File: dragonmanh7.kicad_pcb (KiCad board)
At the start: 4 copper layers, 135.6 x 54.6 mm, 110 parts, among them J1 USB_B, J10 Conn_02x12_Odd_Even, J11 Conn_02x03_Odd_Even, J12 VBAT+, J13 Conn_02x05_Odd_Even, J14 VBATG, J15 Conn_02x02_Odd_Even, J18 Conn_02x05_Odd_Even, J2 73725-0110BLF, J3 RJ45_Amphenol_RJMG1BD3B8K1ANR, J4 Micro_SD_Card, J5 Screw_Terminal_01x06, J6 Conn_02x12_Odd_Even, J7 USB_B, J8 Screw_Terminal_01x02, J9 Conn_02x12_Odd_Even, SW1 RESET, SW2 PC13, U1 STM32H743VITx, U10 USBLC6-2SC6, U12 TCAN332, U13 ISL83483, U14 MIC2005A, U2 KSZ8081RNA, U5 S25FL127SABMFI101, U6 AP63203, U7 USBLC6-2SC6, U8 STM32F042F6Px, U9 USBLC6-2SC6, Y1 8MHz, Y2 32.768KHz, Y3 25MHz

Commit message: Add fidutial for automatic mounting
Signed-off-by: Martin Ribelotta <martinribelotta@gmail.com>
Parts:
- added FID1: Fiducial, Fiducial:Fiducial_1mm_Mask2mm, F.Cu at (83.6, 51.8)
- added FID2: Fiducial, Fiducial:Fiducial_1mm_Mask2mm, F.Cu at (153.9, 70.9)
- added FID3: Fiducial, Fiducial:Fiducial_1mm_Mask2mm, F.Cu at (149.4, 47.8)
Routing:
- net /PE12: track 92.7 -> 89.2 mm
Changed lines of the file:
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@@
     (thickness 1.6)
     (drawings 62)
-    (tracks 4092)
+    (tracks 4091)
     (zones 0)
-    (modules 110)
+    (modules 113)
     (nets 133)
   )
@@
     (add_net VDC)
   )
+  (module Fiducial:Fiducial_1mm_Mask2mm (layer F.Cu)
+    (at 149.352 47.752 90)
+    (descr "Circular Fiducial, 1mm bare copper, 2mm soldermask opening (Level A)")
+    (tags fiducial)
+    (attr smd)
+    (fp_text reference FID3 (at -2.794 0 90) (layer F.SilkS)
+      (effects (font (size 1 1) (thickness 0.15)))
+    )
+    (fp_text value Fiducial (at 0 2 90) (layer F.Fab)
+      (effects (font (size 1 1) (thickness 0.15)))
+    )
+    (fp_circle (center 0 0) (end 1.25 0) (layer F.CrtYd) (width 0.05))
+    (fp_text user %R (at 0 0 90) (layer F.Fab)
+      (effects (font (size 0.4 0.4) (thickness 0.06)))
+    )
+    (fp_circle (center 0 0) (end 1 0) (layer F.Fab) (width 0.1))
+    (pad "" smd circle (at 0 0 90) (size 1 1) (layers F.Cu F.Mask)
+      (solder_mask_margin 0.5) (clearance 0.5))
+  )
+  (module Fiducial:Fiducial_1mm_Mask2mm (layer F.Cu)
+    (at 153.924 70.866)
+    (descr "Circular Fiducial, 1mm bare copper, 2mm soldermask opening (Level A)")
+    (tags fiducial)
+    (attr smd)
+    (fp_text reference FID2 (at 0 -3.048 90) (layer F.SilkS)
+      (effects (font (size 1 1) (thickness 0.15)))
+    )
+    (fp_text value Fiducial (at 0 2) (layer F.Fab)
+      (effects (font (size 1 1) (thickness 0.15)))
+    )
+    (fp_circle (center 0 0) (end 1.25 0) (layer F.CrtYd) (width 0.05))
+    (fp_text user %R (at 0 0) (layer F.Fab)
+      (effects (font (size 0.4 0.4) (thickness 0.06)))
+    )
+    (fp_circle (center 0 0) (end 1 0) (layer F.Fab) (width 0.1))
+    (pad "" smd circle (at 0 0) (size 1 1) (layers F.Cu F.Mask)
+      (solder_mask_margin 0.5) (clearance 0.5))
+  )
+  (module Fiducial:Fiducial_1mm_Mask2mm (layer F.Cu)
+    (at 83.566 51.816 180)
+    (descr "Circular Fiducial, 1mm bare copper, 2mm soldermask opening (Level A)")
+    (tags fiducial)
+    (attr smd)
+    (fp_text reference FID1 (at 1.524 2.032) (layer F.SilkS)
+      (effects (font (size 1 1) (thickness 0.15)))
+    )
+    (fp_text value Fiducial (at 0 2) (layer F.Fab)
+      (effects (font (size 1 1) (thickness 0.15)))
+    )
+    (fp_circle (center 0 0) (end 1.25 0) (layer F.CrtYd) (width 0.05))
+    (fp_text user %R (at 0 0) (layer F.Fab)
+      (effects (font (size 0.4 0.4) (thickness 0.06)))
+    )
+    (fp_circle (center 0 0) (end 1 0) (layer F.Fab) (width 0.1))
+    (pad "" smd circle (at 0 0 180) (size 1 1) (layers F.Cu F.Mask)
+      (solder_mask_margin 0.5) (clearance 0.5))
+  )
   (module Symbol:KiCad-Logo2_8mm_SilkScreen (layer F.Cu)
     (at 104.8766 65.6082)
@@
   (segment (start 131.535119 52.325219) (end 131.13512 51.92522) (width 0.25) (layer F.Cu) (net 90))
   (segment (start 132.545281 55.410141) (end 132.545281 53.335381) (width 0.25) (layer F.Cu) (net 90))
-  (segment (start 178.80566 76.33734) (end 180.5432 74.5998) (width 0.25) (layer F.Cu) (net 90))
-  (segment (start 191.4652 66.04) (end 190.5 66.04) (width 0.25) (layer F.Cu) (net 90))
-  (segment (start 177.96514 76.33734) (end 178.80566 76.33734) (width 0.25) (layer F.Cu) (net 90))
-  (segment (start 180.5432 74.5998) (end 186.05895 74.5998) (width 0.25) (layer F.Cu) (net 90))
-  (segment (start 186.05895 74.5998) (end 187.39329 73.26546) (width 0.25) (layer F.Cu) (net 90))
-  (segment (start 187.39329 73.26546) (end 191.05964 73.26546) (width 0.25) (layer F.Cu) (net 90))
-  (segment (start 191.77508 66.34988) (end 191.4652 66.04) (width 0.25) (layer F.Cu) (net 90))
-  (segment (start 191.77508 72.55002) (end 191.77508 66.34988) (width 0.25) (layer F.Cu) (net 90))
-  (segment (start 191.05964 73.26546) (end 191.77508 72.55002) (width 0.25) (layer F.Cu) (net 90))
   (segment (start 178.273989 54.744189) (end 186.784999 63.255199) (width 0.25) (layer B.Cu) (net 90))
   (segment (start 140.9192 51.92522) (end 143.738169 54.744189) (width 0.25) (layer B.Cu) (net 90))
@@
   (segment (start 186.784999 63.255199) (end 186.784999 64.064001) (width 0.25) (layer B.Cu) (net 90))
   (segment (start 131.13512 51.92522) (end 140.9192 51.92522) (width 0.25) (layer B.Cu) (net 90))
+  (segment (start 189.650001 66.889999) (end 190.5 66.04) (width 0.25) (layer F.Cu) (net 90))
+  (segment (start 177.96514 76.33734) (end 178.80566 76.33734) (width 0.25) (layer F.Cu) (net 90))
+  (segment (start 178.80566 76.33734) (end 180.5432 74.5998) (width 0.25) (layer F.Cu) (net 90))
+  (segment (start 180.5432 74.5998) (end 186.436 74.5998) (width 0.25) (layer F.Cu) (net 90))
+  (segment (start 186.436 74.5998) (end 189.1538 71.882) (width 0.25) (layer F.Cu) (net 90))
+  (segment (start 189.1538 71.882) (end 189.1538 70.4596) (width 0.25) (layer F.Cu) (net 90))
+  (segment (start 189.135001 67.404999) (end 189.650001 66.889999) (width 0.25) (layer F.Cu) (net 90))
+  (segment (start 189.1538 70.4596) (end 189.135001 67.404999) (width 0.25) (layer F.Cu) (net 90))
   (via (at 132.34162 50.7873) (size 0.8) (drill 0.4) (layers F.Cu B.Cu) (net 91))
   (segment (start 133.045281 51.490961) (end 132.34162 50.7873) (width 0.25) (layer F.Cu) (net 91))

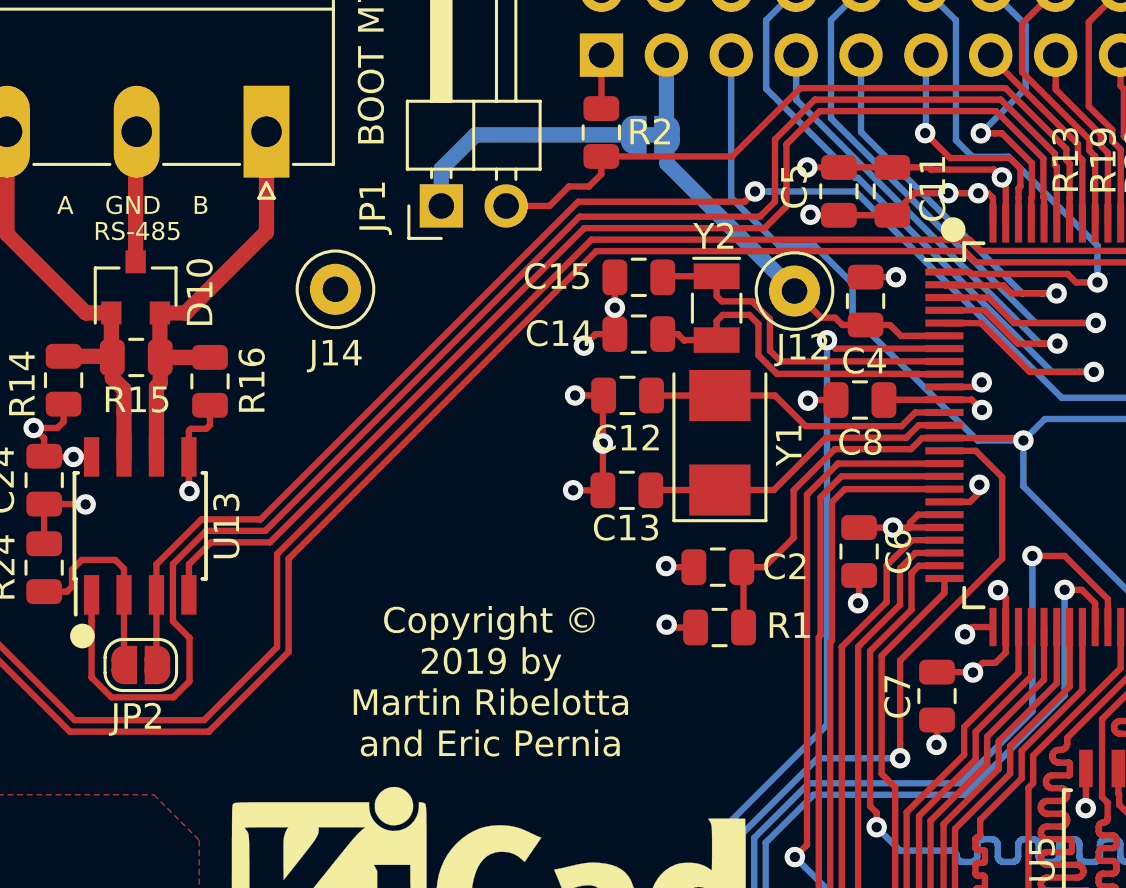
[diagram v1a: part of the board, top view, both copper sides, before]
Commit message: Improve oscilator ground
Signed-off-by: Martin Ribelotta <martinribelotta@gmail.com>
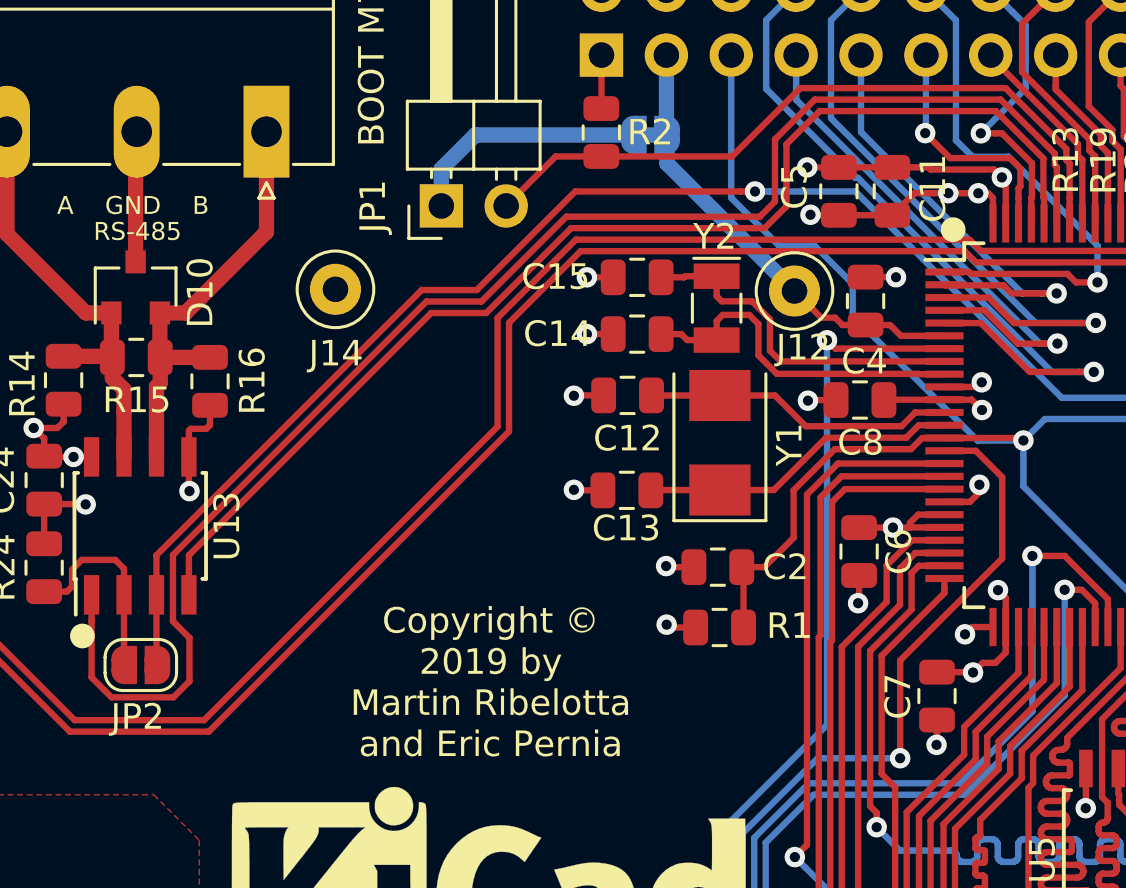
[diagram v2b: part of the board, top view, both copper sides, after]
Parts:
- moved C14 0.06 mm to (110.6, 43.9)
- moved C15 0.06 mm to (110.6, 41.7)
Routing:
- net GND: track 175.0 -> 169.7 mm, vias 57 -> 56

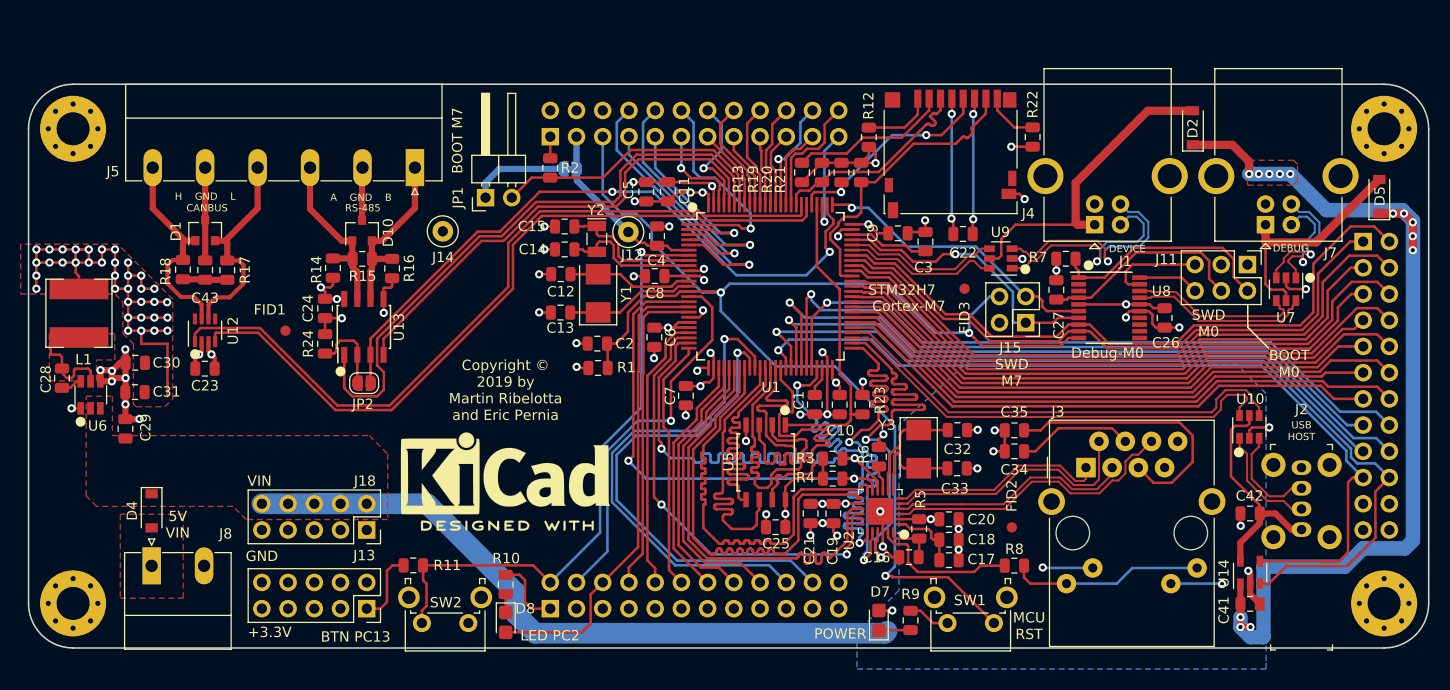
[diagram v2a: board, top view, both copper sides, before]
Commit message: Add voltage testpoints
Signed-off-by: Martin Alejandro Ribelotta <martinribelotta@gmail.com>
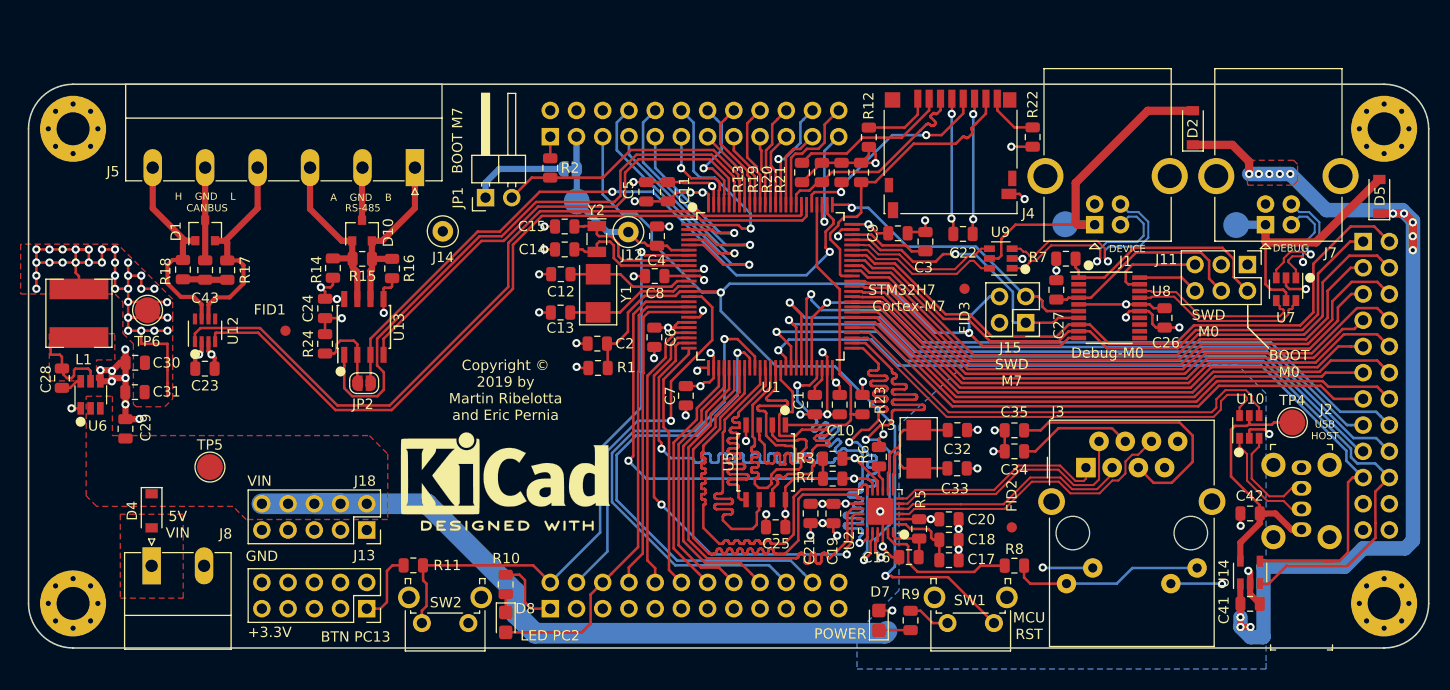
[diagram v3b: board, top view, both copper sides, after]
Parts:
- added TP1: VBAT_TP, TestPoint:TestPoint_Pad_D2.5mm, B.Cu at (111.8, 39.3)
- added TP2: VBUS1_TP, TestPoint:TestPoint_Pad_D2.5mm, B.Cu at (159.1, 41.5)
- added TP3: VBUS2_TP, TestPoint:TestPoint_Pad_D2.5mm, B.Cu at (175.7, 41.6)
- added TP4: VBUS3_TP, TestPoint:TestPoint_Pad_D2.5mm, F.Cu at (181.1, 60.7)
- added TP5: VIN_TP, TestPoint:TestPoint_Pad_D2.5mm, F.Cu at (76.3, 65.0)
- added TP6: 3V3_TP, TestPoint:TestPoint_Pad_D2.5mm, F.Cu at (70.2, 49.8)
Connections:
- J3 pad R7: (no net) -> Net-(J3-PadR7)
- U12 pad 5: (no net) -> Net-(U12-Pad5)
- U12 pad 8: (no net) -> Net-(U12-Pad8)
- U2 pad 17: (no net) -> Net-(U2-Pad17)
- U2 pad 18: (no net) -> Net-(U2-Pad18)
- U8 pad 11: (no net) -> Net-(U8-Pad11)
- U8 pad 12: (no net) -> Net-(U8-Pad12)
- U8 pad 13: (no net) -> Net-(U8-Pad13)
- U8 pad 14: (no net) -> Net-(U8-Pad14)
- U8 pad 2: (no net) -> Net-(U8-Pad2)
- U8 pad 3: (no net) -> Net-(U8-Pad3)
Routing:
- net /VBUS3: track 22.2 -> 26.5 mm
- net /VBUS1: track 32.5 -> 35.4 mm
- net /VBUS2: track 24.1 -> 27.0 mm
- net +BATT: track 17.9 -> 19.1 mm
- net +3V3: vias 61 -> 57
